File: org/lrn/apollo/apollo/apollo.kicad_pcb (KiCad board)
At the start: 2 copper layers, 2 x 7.5 mm, 88 parts, among them J10 Conn_01x01_Male, J11 Conn_01x01_Male, J12 Conn_01x01_Male, J13 Conn_01x01_Male, J17 Conn_01x01_Male, J18 Conn_01x01_Male, J4 Conn_01x01_Male, J6 Conn_01x01_Male, J7 Conn_01x01_Male, J8 Conn_01x01_Male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

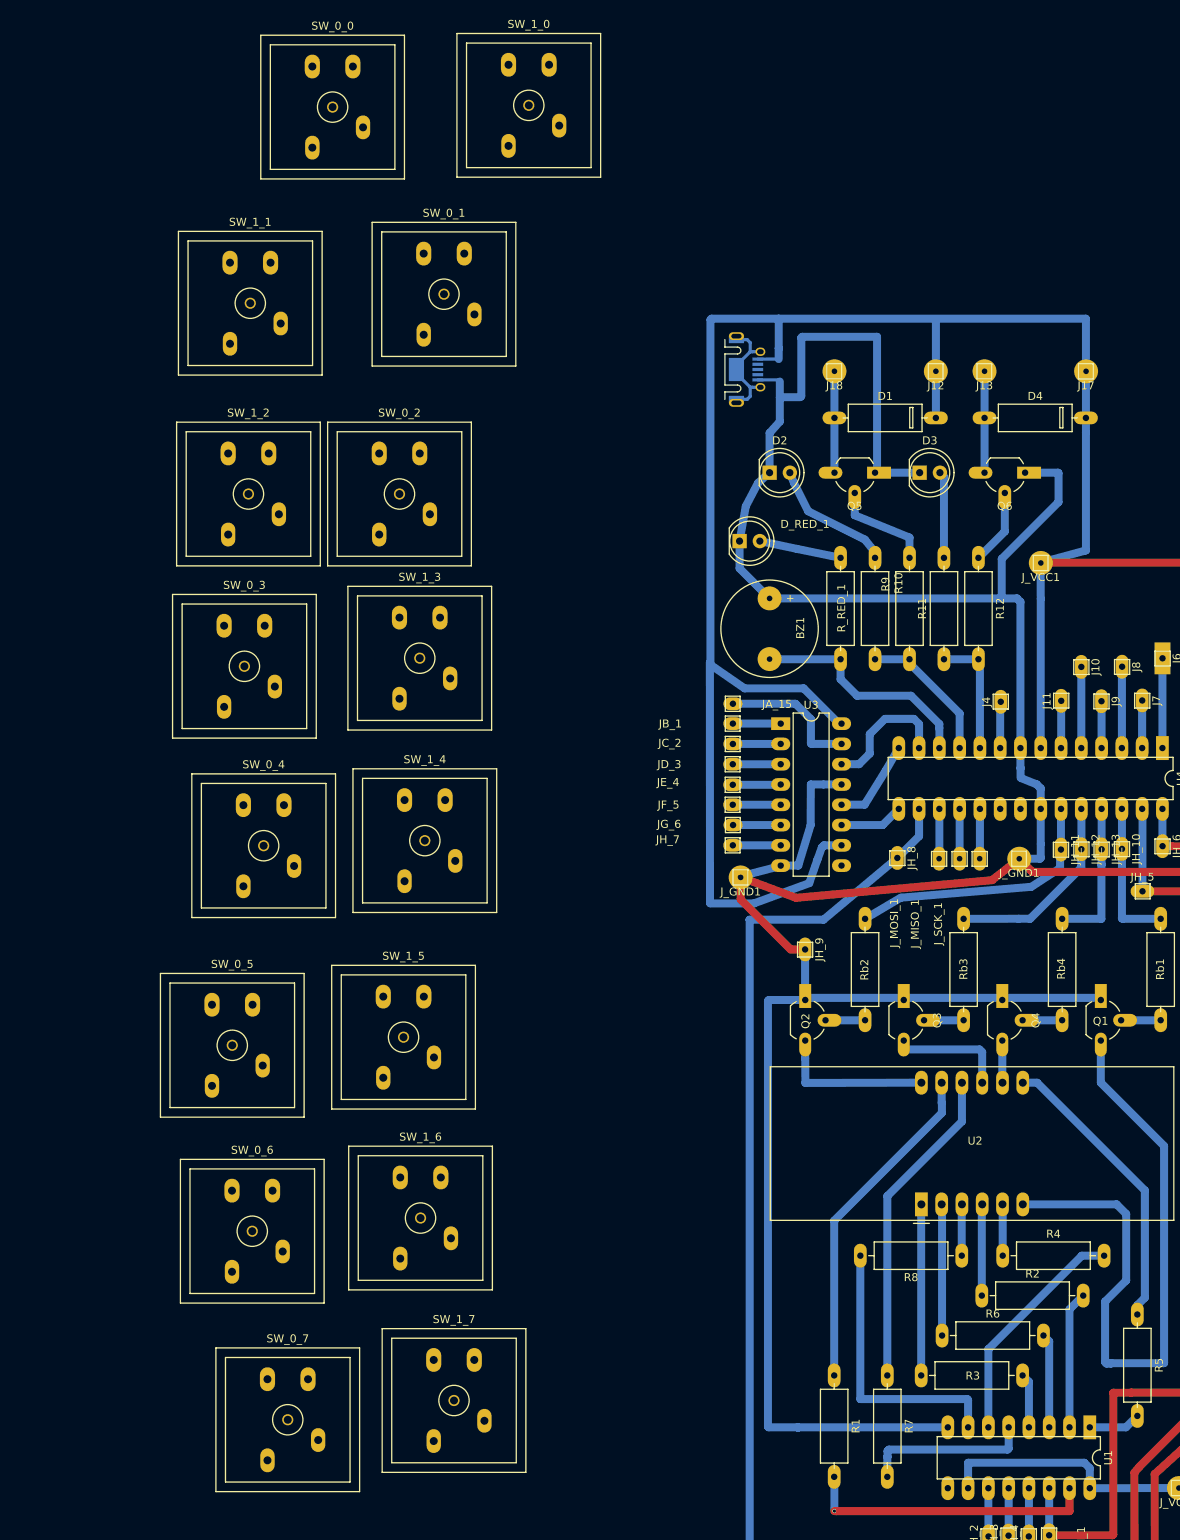
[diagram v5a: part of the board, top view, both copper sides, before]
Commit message: apollo: keubord linked in pcb
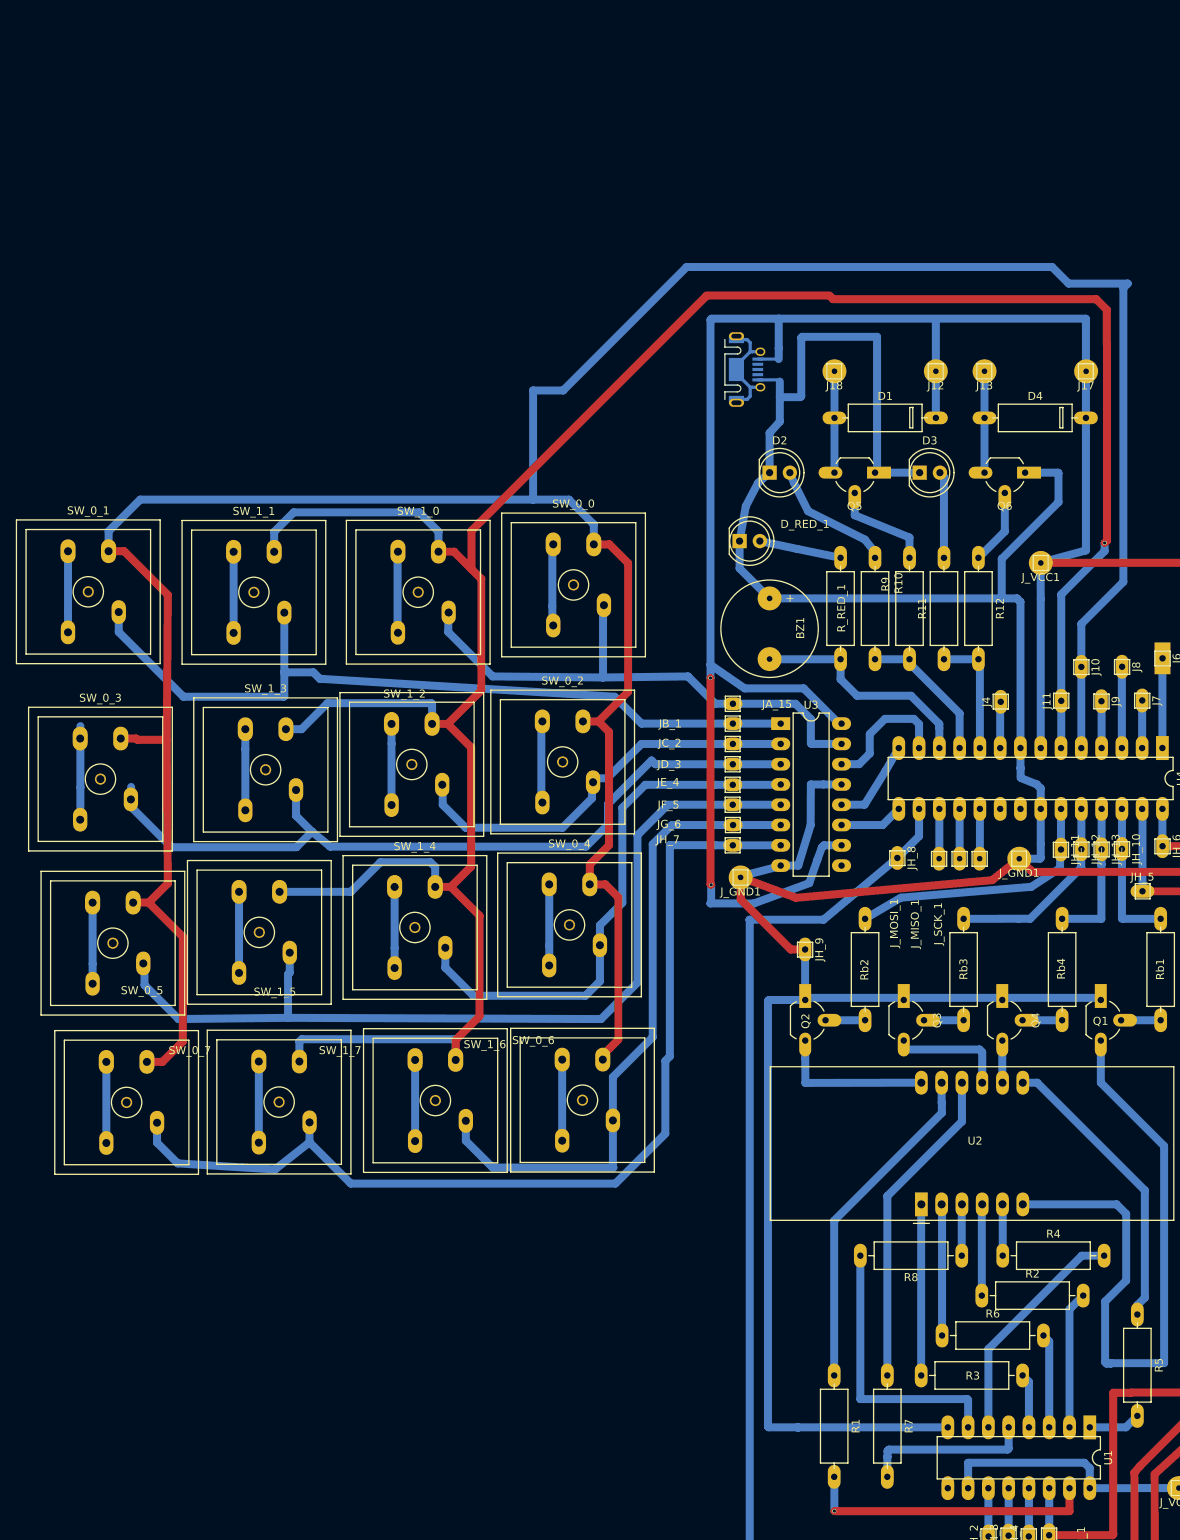
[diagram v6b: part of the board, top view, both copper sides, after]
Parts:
- moved SW_0_0 67.0 mm to (-1.01, 48.3)
- moved SW_1_0 62.5 mm to (-20.5, 49.2)
- moved SW_0_1 58.1 mm to (-61.8, 49.2)
- moved SW_0_7 44.6 mm to (-57.0, 113.1)
- moved SW_0_6 44.5 mm to (0.12, 112.8)
- moved SW_1_7 43.3 mm to (-37.9, 113.1)
- moved SW_1_2 39.6 mm to (-21.3, 70.8)
- moved SW_0_4 39.6 mm to (-1.51, 90.9)
- moved SW_0_2 39.3 mm to (-2.37, 70.5)
- moved SW_1_1 36.2 mm to (-41.0, 49.2)
- moved SW_1_3 23.8 mm to (-39.6, 71.5)
- moved SW_0_3 22.9 mm to (-60.3, 72.6)
- moved SW_1_5 22.3 mm to (-40.4, 91.8)
- moved SW_0_5 19.7 mm to (-58.7, 93.2)
- moved SW_1_6 14.8 mm to (-18.3, 112.9)
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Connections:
- SW_0_3 pad 4: Net-(SW_0_3-Pad4) -> Net-(J10-Pad1)
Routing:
- net Net-(J10-Pad1): track 10.2 -> 382.4 mm
- net Net-(J11-Pad1): track 5.92 -> 330.6 mm, vias 0 -> 1
- net Net-(JH_7-Pad1): track 6.00 -> 125.9 mm
- net Net-(JF_5-Pad1): track 6.01 -> 114.1 mm
- net Net-(JB_1-Pad1): track 6.00 -> 101.1 mm
- net Net-(JD_3-Pad1): track 6.01 -> 99.7 mm
- net Net-(JG_6-Pad1): track 5.97 -> 82.0 mm
- net Net-(JE_4-Pad1): track 6.08 -> 68.1 mm
- net Net-(JA_15-Pad1): track 17.5 -> 68.3 mm
- net Net-(JC_2-Pad1): track 6.00 -> 51.9 mm
- net Net-(SW_1_6-Pad2): track 0.00 -> 10.2 mm
- net Net-(SW_0_7-Pad2): track 0.00 -> 10.2 mm
- net Net-(SW_1_7-Pad2): track 0.00 -> 10.2 mm
- net Net-(SW_1_5-Pad2): track 0.00 -> 10.2 mm
- net Net-(SW_1_4-Pad2): track 0.00 -> 10.2 mm
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
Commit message: apollo: keyboard pcb regularization
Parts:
- added REF**: Pin_D1.0mm_L10.0mm, Connector_Pin:Pin_D1.0mm_L10.0mm, F.Cu at (84.5, 159.3)
- added REF**: Pin_D1.0mm_L10.0mm, Connector_Pin:Pin_D1.0mm_L10.0mm, F.Cu at (104.0, 139.4)
- added REF**: Pin_D1.0mm_L10.0mm, Connector_Pin:Pin_D1.0mm_L10.0mm, F.Cu at (104.0, 119.3)
- added REF**: Pin_D1.0mm_L10.0mm, Connector_Pin:Pin_D1.0mm_L10.0mm, F.Cu at (104.0, 99.3)
- added REF**: Pin_D1.0mm_L10.0mm, Connector_Pin:Pin_D1.0mm_L10.0mm, F.Cu at (44.5, 159.3)
- added REF**: Pin_D1.0mm_L10.0mm, Connector_Pin:Pin_D1.0mm_L10.0mm, F.Cu at (44.5, 139.3)
- added REF**: Pin_D1.0mm_L10.0mm, Connector_Pin:Pin_D1.0mm_L10.0mm, F.Cu at (44.5, 119.4)
- added REF**: Pin_D1.0mm_L10.0mm, Connector_Pin:Pin_D1.0mm_L10.0mm, F.Cu at (44.5, 99.3)
- added REF**: Pin_D1.0mm_L10.0mm, Connector_Pin:Pin_D1.0mm_L10.0mm, F.Cu at (84.4, 139.3)
- added REF**: Pin_D1.0mm_L10.0mm, Connector_Pin:Pin_D1.0mm_L10.0mm, F.Cu at (84.5, 119.2)
- added REF**: Pin_D1.0mm_L10.0mm, Connector_Pin:Pin_D1.0mm_L10.0mm, F.Cu at (84.5, 99.3)
- added REF**: Pin_D1.0mm_L10.0mm, Connector_Pin:Pin_D1.0mm_L10.0mm, F.Cu at (64.4, 159.3)
- added REF**: Pin_D1.0mm_L10.0mm, Connector_Pin:Pin_D1.0mm_L10.0mm, F.Cu at (64.5, 139.2)
- added REF**: Pin_D1.0mm_L10.0mm, Connector_Pin:Pin_D1.0mm_L10.0mm, F.Cu at (64.5, 119.3)
- added REF**: Pin_D1.0mm_L10.0mm, Connector_Pin:Pin_D1.0mm_L10.0mm, F.Cu at (64.5, 99.3)
- added REF**: Pin_D1.0mm_L10.0mm, Connector_Pin:Pin_D1.0mm_L10.0mm, F.Cu at (104.1, 159.3)
- moved SW_0_1 111.0 mm to (34.5, 104.4)
- moved SW_0_2 110.8 mm to (94.5, 124.4)
- moved SW_0_0 110.7 mm to (94.5, 104.4)
- moved SW_1_1 110.3 mm to (54.5, 104.4)
- moved SW_0_4 109.9 mm to (94.5, 144.4)
- moved SW_1_0 109.8 mm to (74.5, 104.4)
- moved SW_1_2 109.7 mm to (74.5, 124.4)
- moved SW_1_4 109.2 mm to (74.5, 144.4)
- moved SW_1_5 108.4 mm to (54.5, 144.4)
- moved SW_0_3 108.0 mm to (34.5, 124.4)
- moved SW_1_3 107.9 mm to (54.5, 124.4)
- moved SW_0_6 107.5 mm to (94.5, 164.4)
- moved SW_0_5 106.3 mm to (34.5, 144.4)
- moved SW_1_6 106.1 mm to (74.5, 164.4)
- moved SW_1_7 105.7 mm to (54.5, 164.4)
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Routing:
- net Net-(J11-Pad1): track 330.6 -> 446.3 mm
- net Net-(J10-Pad1): track 382.4 -> 453.4 mm
- net Net-(JC_2-Pad1): track 51.9 -> 122.8 mm
- net Net-(JG_6-Pad1): track 82.0 -> 152.7 mm
- net Net-(JE_4-Pad1): track 68.1 -> 137.7 mm
- net Net-(JH_7-Pad1): track 125.9 -> 193.4 mm
- net Net-(JF_5-Pad1): track 114.1 -> 178.3 mm
- net Net-(JD_3-Pad1): track 99.7 -> 163.4 mm
- net Net-(JA_15-Pad1): track 68.3 -> 119.4 mm
- net Net-(JB_1-Pad1): track 101.1 -> 148.6 mm
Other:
- outline, holes or cut-outs redrawn

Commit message: replace R100-Ohm resistors for 7-segment to smd
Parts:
- added REF**: Pin_D1.0mm_L10.0mm, Connector_Pin:Pin_D1.0mm_L10.0mm, F.Cu at (164.3, 119.8)
- added REF**: Pin_D1.0mm_L10.0mm, Connector_Pin:Pin_D1.0mm_L10.0mm, F.Cu at (169.4, 117.5)
- added REF**: Pin_D1.0mm_L10.0mm, Connector_Pin:Pin_D1.0mm_L10.0mm, F.Cu at (137.6, 117.5)
- added REF**: Pin_D1.0mm_L10.0mm, Connector_Pin:Pin_D1.0mm_L10.0mm, F.Cu at (171.8, 119.8)
- added REF**: Pin_D1.0mm_L10.0mm, Connector_Pin:Pin_D1.0mm_L10.0mm, F.Cu at (174.0, 122.2)
- added REF**: Pin_D1.0mm_L10.0mm, Connector_Pin:Pin_D1.0mm_L10.0mm, F.Cu at (158.5, 122.2)
- added REF**: Pin_D1.0mm_L10.0mm, Connector_Pin:Pin_D1.0mm_L10.0mm, F.Cu at (178.4, 128.5)
- added REF**: Pin_D1.0mm_L10.0mm, Connector_Pin:Pin_D1.0mm_L10.0mm, F.Cu at (162.6, 128.5)
- R1, R2, R3, R4, R5, R6, R7, R8: footprint apollo:R__Horizontal -> Resistor_SMD:R_1206_3216Metric_Pad1.42x1.75mm_HandSolder; moved to B.Cu
- moved R7 42.4 mm to (165.1, 114.1), turned to 0 degrees
- moved R1 33.7 mm to (132.5, 116.4), turned to 180 degrees
- moved R5 33.2 mm to (163.7, 110.7), turned to 0 degrees
- moved R3 26.5 mm to (143.3, 123.6), turned to 90 degrees
- moved JH_1 21.8 mm to (171.2, 149.8)
- moved JH_2 21.8 mm to (163.6, 150.0)
- moved JH_3 21.8 mm to (166.1, 149.9)
- moved JH_4 21.8 mm to (168.6, 150.0)
- moved U1 21.8 mm to (176.2, 136.3)
- moved R6 21.3 mm to (149.2, 123.6), turned to 90 degrees
- moved R2 16.3 mm to (154.3, 123.6), turned to 90 degrees
- moved R4 11.7 mm to (163.1, 125.0)
- moved R8 2.47 mm to (153.3, 133.0), turned to 0 degrees
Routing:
- net Net-(R1-Pad2): track 36.6 -> 94.2 mm, vias 1 -> 2
- net Net-(R3-Pad2): track 6.83 -> 58.3 mm
- net Net-(Q1-Pad3): track 84.3 -> 49.6 mm
- net Net-(R5-Pad1): track 36.8 -> 3.50 mm
- net Net-(R6-Pad2): track 11.8 -> 41.8 mm
- net Net-(R5-Pad2): track 6.55 -> 35.5 mm
- net Net-(JH_3-Pad1): track 152.7 -> 126.5 mm
- net Net-(R8-Pad2): track 34.9 -> 9.54 mm
- net Net-(R7-Pad1): track 40.5 -> 15.8 mm
- net Net-(JH_1-Pad1): track 121.1 -> 99.6 mm, vias 0 -> 1
- net Net-(R1-Pad1): track 42.3 -> 21.0 mm
- net Net-(R2-Pad2): track 17.2 -> 34.1 mm
- net Net-(R4-Pad2): track 29.1 -> 12.4 mm
- net Net-(R3-Pad1): track 21.4 -> 4.79 mm
- net Net-(R6-Pad1): track 16.4 -> 3.40 mm
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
